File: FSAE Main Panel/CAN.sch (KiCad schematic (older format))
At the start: 8 parts, among them U401 MCP2515-I/ST, U402 MCP2551-I/SN, Y401 16MHz

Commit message: New footprints, finished associating footprints
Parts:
- Y401: footprint (none) -> CSTNE16M0V530000R0:CSTNE16M0V530000R0
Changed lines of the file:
@@
 F 0 "Y401" H 3400 3900 50  0000 C CNN
 F 1 "16MHz" H 3400 3600 50  0000 C CNN
-F 2 "" H 3400 3750 50  0001 C CNN
+F 2 "CSTNE16M0V530000R0:CSTNE16M0V530000R0" H 3400 3750 50  0001 C CNN
 F 3 "" H 3400 3750 50  0001 C CNN
 	1    3400 3750

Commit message: Edited footprints, started PCB layout
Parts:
- removed C401, C402: 22pF, Capacitors_SMD:C_1206, symbol Device:C
- removed Y401: 16MHz, CSTNE16M0V530000R0:CSTNE16M0V530000R0, symbol Device:Crystal
- added Y401: Resonator, CSTNE16M0V530000R0:CSTNE16M0V530000R0, symbol Device:Resonator
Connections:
- wire segments 38 -> 35
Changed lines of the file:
@@
 $EndComp
-$Comp
-L Device:Crystal Y401
-U 1 1 5BE251BE
-P 3400 3750
-F 0 "Y401" H 3400 3900 50  0000 C CNN
-F 1 "16MHz" H 3400 3600 50  0000 C CNN
-F 2 "CSTNE16M0V530000R0:CSTNE16M0V530000R0" H 3400 3750 50  0001 C CNN
-F 3 "" H 3400 3750 50  0001 C CNN
-	1    3400 3750
-	0    -1   -1   0
-$EndComp
-Wire Wire Line
-	3000 3600 3400 3600
-Wire Wire Line
-	4100 3700 3650 3700
-Wire Wire Line
-	3650 3700 3650 3900
-Wire Wire Line
-	3650 3900 3400 3900
-$Comp
-L Device:C C401
-U 1 1 5BE2525F
-P 2850 3600
-F 0 "C401" V 2750 3700 50  0000 L CNN
-F 1 "22pF" V 2750 3350 50  0000 L CNN
-F 2 "Capacitors_SMD:C_1206" H 2888 3450 50  0001 C CNN
-F 3 "" H 2850 3600 50  0001 C CNN
-F 4 "Ceramic 22pF 10V C0G/NG0 0805" V 2850 3600 50  0001 C CNN "Description"
-	1    2850 3600
-	0    1    1    0
-$EndComp
-$Comp
-L Device:C C402
-U 1 1 5BE2528F
-P 2850 3900
-F 0 "C402" V 2750 4000 50  0000 L CNN
-F 1 "22pF" V 2750 3650 50  0000 L CNN
-F 2 "Capacitors_SMD:C_1206" H 2888 3750 50  0001 C CNN
-F 3 "" H 2850 3900 50  0001 C CNN
-F 4 "Ceramic 22pF 10V C0G/NG0 0805" V 2850 3900 50  0001 C CNN "Description"
-	1    2850 3900
-	0    1    1    0
-$EndComp
-Connection ~ 3400 3600
-Connection ~ 3400 3900
 $Comp
 L power:GND #PWR0401
 U 1 1 5BE2541F
-P 2400 4600
-F 0 "#PWR0401" H 2400 4350 50  0001 C CNN
-F 1 "GND" H 2400 4450 50  0000 C CNN
-F 2 "" H 2400 4600 50  0001 C CNN
-F 3 "" H 2400 4600 50  0001 C CNN
-	1    2400 4600
+P 3400 4550
+F 0 "#PWR0401" H 3400 4300 50  0001 C CNN
+F 1 "GND" H 3400 4400 50  0000 C CNN
+F 2 "" H 3400 4550 50  0001 C CNN
+F 3 "" H 3400 4550 50  0001 C CNN
+	1    3400 4550
 	1    0    0    -1
 $EndComp
-Wire Wire Line
-	2700 3600 2400 3600
-Wire Wire Line
-	2400 3600 2400 3900
-Wire Wire Line
-	2700 3900 2400 3900
-Connection ~ 2400 3900
 $Comp
 L power:+3.3V #PWR0402
@@
 	4700 4200 4700 4350
 Wire Wire Line
-	4700 4350 2400 4350
-Connection ~ 2400 4350
+	4700 4350 3400 4350
 $Comp
 L FSAE-Main-Panel-rescue:MCP2551-I_SN U402
@@
 NoConn ~ 4100 3800
 Wire Wire Line
-	3400 3600 4100 3600
-Wire Wire Line
-	3400 3900 3000 3900
-Wire Wire Line
-	2400 3900 2400 4350
-Wire Wire Line
-	2400 4350 2400 4600
-Wire Wire Line
 	4700 2400 4700 2600
 Wire Wire Line
@@
 Wire Wire Line
 	6000 2400 7200 2400
+$Comp
+L Device:Resonator Y401
+U 1 1 5C382AA1
+P 3400 3700
+F 0 "Y401" H 3400 3948 50  0000 C CNN
+F 1 "Resonator" H 3400 3857 50  0000 C CNN
+F 2 "CSTNE16M0V530000R0:CSTNE16M0V530000R0" H 3375 3700 50  0001 C CNN
+F 3 "~" H 3375 3700 50  0001 C CNN
+	1    3400 3700
+	-1   0    0    -1
+$EndComp
+Wire Wire Line
+	3250 3700 3100 3700
+Wire Wire Line
+	3100 3700 3100 3300
+Wire Wire Line
+	3100 3300 3800 3300
+Wire Wire Line
+	3800 3300 3800 3600
+Wire Wire Line
+	3800 3600 4100 3600
+Wire Wire Line
+	3550 3700 4100 3700
+Connection ~ 3400 4350
+Wire Wire Line
+	3400 4350 3400 4550
+Wire Wire Line
+	3400 3900 3400 4350
 $EndSCHEMATC

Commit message: Updated PCB
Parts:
- U401: footprint Housings_SSOP:TSSOP-20_4.4x6.5mm_Pitch0.65mm -> Housings_SOIC:SOIC-18W_7.5x11.6mm_Pitch1.27mm; symbol FSAE-Main-Panel-rescue:MCP2515-I_ST -> Interface_CAN_LIN:MCP2515-xSO
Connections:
- net +3V3: now also U401.18 (VDD); no longer U401.20 (VDD)
- net CAN_CS: now also U401.16 (~CS); no longer U401.18 (~CS)
- net CAN_MISO: now also U401.15 (SO); no longer U401.17 (SO)
- net CAN_MOSI: now also U401.14 (SI); no longer U401.16 (SI)
- net CAN_SCLK: now also U401.13 (SCK); no longer U401.14 (SCK)
- net GND: now also U401.9 (VSS); no longer U401.10 (VSS)
- net at R401.2: now also U401.17 (~RESET); no longer U401.19 (~RESET)
- net at U401.7 (OSC2): now also Y401.3
- net at U401.8 (OSC1): now also Y401.1; no longer Y401.3
- no-connect marks 2 -> 8
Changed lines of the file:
@@
 $EndDescr
 $Comp
-L FSAE-Main-Panel-rescue:MCP2515-I_ST U401
+L Interface_CAN_LIN:MCP2515-xSO U401
 U 1 1 5BE2515F
 P 4700 3400
 F 0 "U401" H 4300 4175 50  0000 R CNN
 F 1 "MCP2515-I/ST" H 5450 4200 50  0000 R TNN
-F 2 "Housings_SSOP:TSSOP-20_4.4x6.5mm_Pitch0.65mm" H 4700 2500 50  0001 C CIN
+F 2 "Housings_SOIC:SOIC-18W_7.5x11.6mm_Pitch1.27mm" H 4700 2500 50  0001 C CIN
 F 3 "" H 4800 2600 50  0001 C CNN
 	1    4700 3400
@@
 Wire Wire Line
 	3400 3900 3400 4350
+NoConn ~ 5300 3400
+NoConn ~ 5300 3500
+NoConn ~ 5300 3600
+NoConn ~ 5300 3700
+NoConn ~ 5300 3800
+NoConn ~ 5300 3900
 $EndSCHEMATC

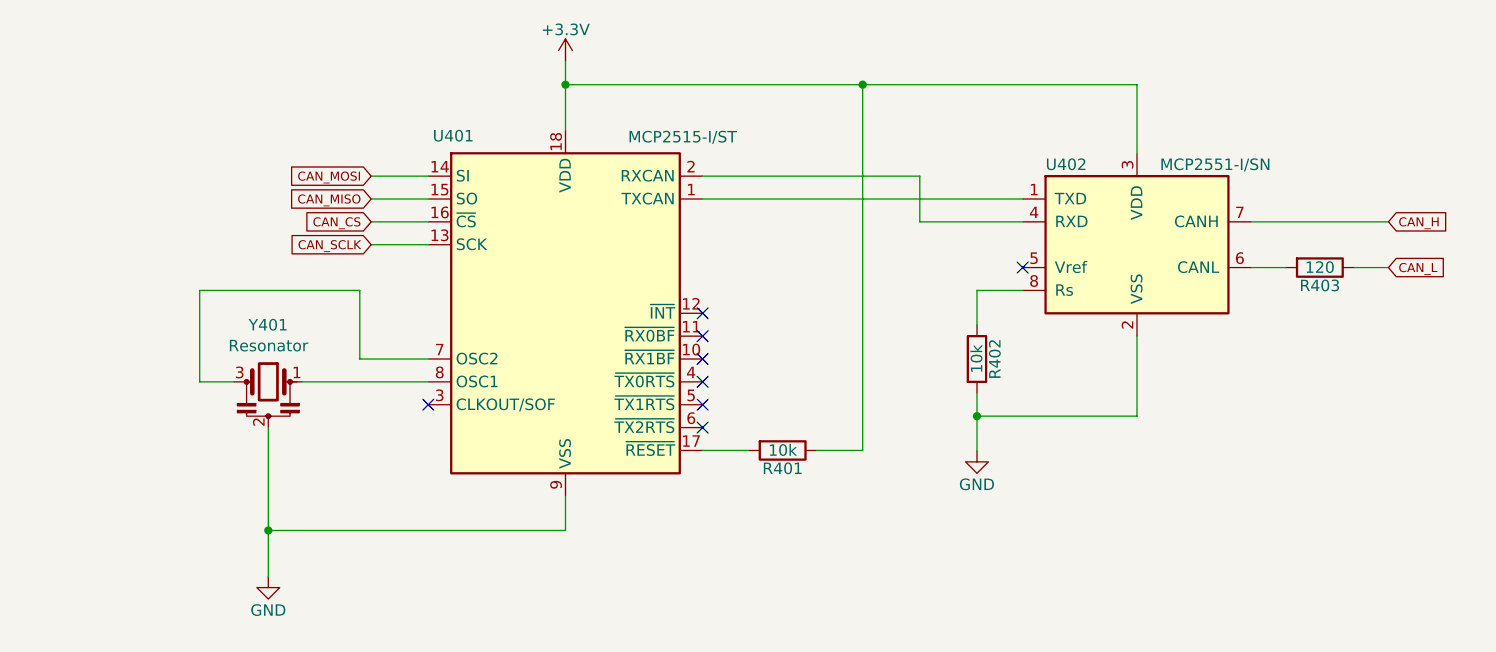
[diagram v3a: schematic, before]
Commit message: Major Revision
Deleted a ton of routes, Sorry Gary.
Changed all LEDs to 1206s for better brightness
Added a lot of local net names for easier routing
Flipped J203 for better routing
Expanded board outline to fit final dashboard cutout
Added half of the Mounting Holes
Realigned RPM strip
Added Linear Reg Load Resistors to meet minimum current specs
Changed Aux load Linear Regulators to a better one
Added Separate Linear Reg for the DWC
Tuned the CAN Bus differential Pair Lines for equal length
Added decoupling capacitors at a few locations
Rerouted Power traces to be shorter and cleaner
Set up keep out zones for CAN bus interference shielding.
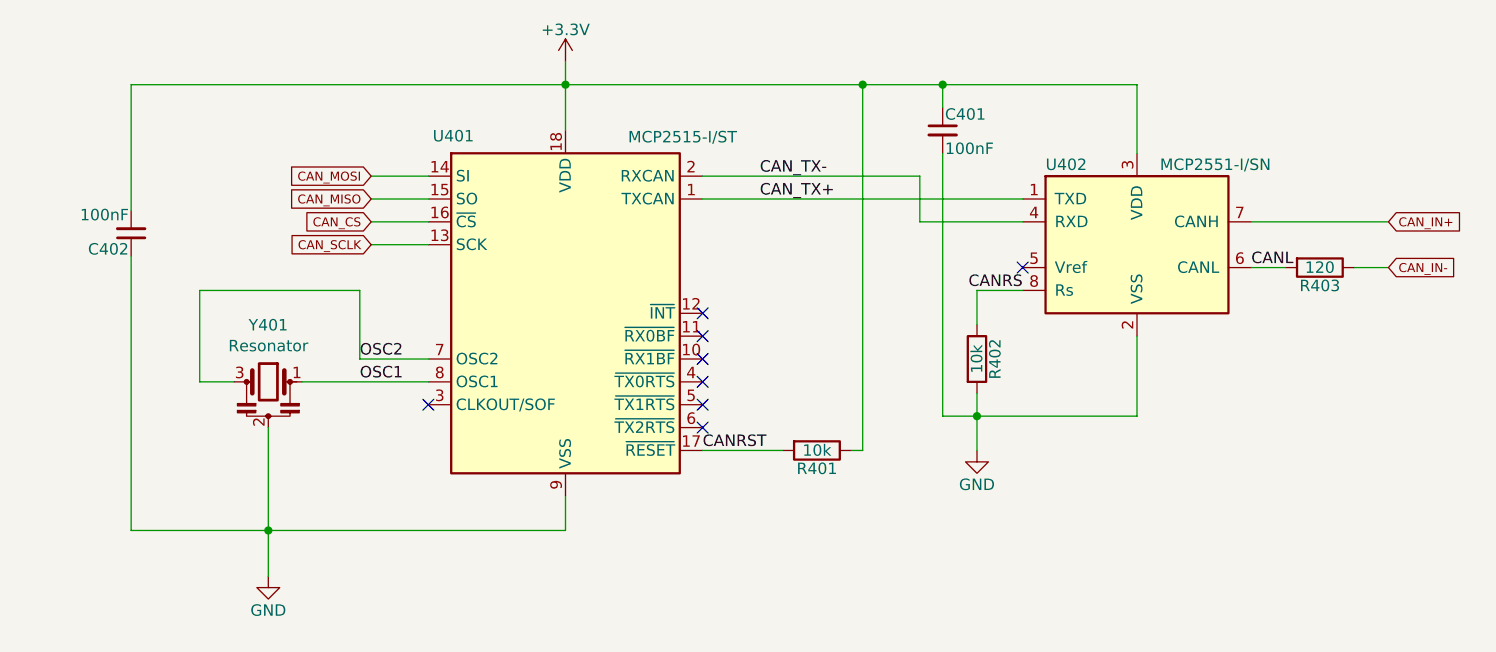
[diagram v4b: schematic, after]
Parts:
- added C401, C402: 100nF, Capacitors_SMD:C_1206, symbol Device:C_Small
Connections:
- net +3V3: now also C401.1, C402.2
- net GND: now also C401.2, C402.1
- net CAN_TX+: now reaches U401.1 (TXCAN), U402.1 (TXD)
- net CANRST: now reaches R401.2, U401.17 (~RESET)
- net CAN_TX-: now reaches U401.2 (RXCAN), U402.4 (RXD)
- net OSC2: now reaches U401.7 (OSC2), Y401.3
- net OSC1: now reaches U401.8 (OSC1), Y401.1
- net CANL: now reaches R403.2, U402.6 (CANL)
- net CANRS: now reaches R402.1, U402.8 (Rs)
- net CAN_H renamed CAN_IN+
- net CAN_L renamed CAN_IN-
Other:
- moved on the sheet: R401
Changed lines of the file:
@@
 L Device:R R401
 U 1 1 5BE255B1
-P 5650 4000
-F 0 "R401" V 5730 4000 50  0000 C CNN
-F 1 "10k" V 5650 4000 50  0000 C CNN
-F 2 "Resistors_SMD:R_1206" V 5580 4000 50  0001 C CNN
-F 3 "" H 5650 4000 50  0001 C CNN
-	1    5650 4000
+P 5800 4000
+F 0 "R401" V 5880 4000 50  0000 C CNN
+F 1 "10k" V 5800 4000 50  0000 C CNN
+F 2 "Resistors_SMD:R_1206" V 5730 4000 50  0001 C CNN
+F 3 "" H 5800 4000 50  0001 C CNN
+	1    5800 4000
 	0    1    1    0
 $EndComp
 Wire Wire Line
-	5500 4000 5300 4000
-Wire Wire Line
-	5800 4000 6000 4000
+	5650 4000 5300 4000
+Wire Wire Line
+	5950 4000 6000 4000
 Wire Wire Line
 	6000 4000 6000 2400
@@
 $EndComp
 Text GLabel 8300 3000 2    39   Input ~ 0
-CAN_H
+CAN_IN+
 Text GLabel 8300 3200 2    39   Input ~ 0
-CAN_L
+CAN_IN-
 Wire Wire Line
 	7700 3000 8300 3000
@@
 	6500 3850 6500 4000
 Wire Wire Line
-	6000 2400 7200 2400
+	6000 2400 6350 2400
 $Comp
 L Device:Resonator Y401
@@
 NoConn ~ 5300 3800
 NoConn ~ 5300 3900
+Text Label 5550 2800 0    50   ~ 0
+CAN_TX-
+Text Label 5550 2900 0    50   ~ 0
+CAN_TX+
+Text Label 3800 3600 0    50   ~ 0
+OSC2
+Text Label 3800 3700 0    50   ~ 0
+OSC1
+Text Label 6700 3300 2    50   ~ 0
+CANRS
+Text Label 7700 3200 0    50   ~ 0
+CANL
+Text Label 5300 4000 0    50   ~ 0
+CANRST
+$Comp
+L Device:C_Small C?
+U 1 1 5C806C3C
+P 6350 2600
+AR Path="/5C806C3C" Ref="C?"  Part="1"
+AR Path="/5BE25053/5C806C3C" Ref="C401"  Part="1"
+F 0 "C401" H 6360 2670 50  0000 L CNN
+F 1 "100nF" H 6360 2520 50  0000 L CNN
+F 2 "Capacitors_SMD:C_1206" H 6350 2600 50  0001 C CNN
+F 3 "" H 6350 2600 50  0001 C CNN
+F 4 "Ceramic 0.1uF 10V X7R 1206" H 6350 2600 50  0001 C CNN "Description"
+	1    6350 2600
+	1    0    0    -1
+$EndComp
+$Comp
+L Device:C_Small C?
+U 1 1 5C8072C7
+P 2800 3050
+AR Path="/5C8072C7" Ref="C?"  Part="1"
+AR Path="/5BE25053/5C8072C7" Ref="C402"  Part="1"
+F 0 "C402" H 2810 3120 50  0000 L CNN
+F 1 "100nF" H 2810 2970 50  0000 L CNN
+F 2 "Capacitors_SMD:C_1206" H 2800 3050 50  0001 C CNN
+F 3 "" H 2800 3050 50  0001 C CNN
+F 4 "Ceramic 0.1uF 10V X7R 1206" H 2800 3050 50  0001 C CNN "Description"
+	1    2800 3050
+	-1   0    0    1
+$EndComp
+Wire Wire Line
+	6350 2500 6350 2400
+Connection ~ 6350 2400
+Wire Wire Line
+	6350 2400 7200 2400
+Wire Wire Line
+	6350 2700 6350 3850
+Wire Wire Line
+	6350 3850 6500 3850
+Wire Wire Line
+	2800 2950 2800 2400
+Wire Wire Line
+	2800 2400 4700 2400
+Wire Wire Line
+	2800 4350 3400 4350
+Wire Wire Line
+	2800 3150 2800 4350
 $EndSCHEMATC

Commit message: Initial Fabrication
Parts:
- R402: value 10k -> 16.9k
- R403: footprint Resistors_SMD:R_1206 -> Resistors_SMD:R_0805
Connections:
- net +3V3: no longer C401.1, U402.3 (VDD)
- net CAN_IN+: now also R403.2
- net CAN_IN-: now also U402.6 (CANL)
- removed net CANL: R403.2, U402.6 (CANL)
- new net +5V: C401.1, U402.3 (VDD)
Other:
- moved on the sheet: R403
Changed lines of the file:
@@
 P 6500 3600
 F 0 "R402" V 6580 3600 50  0000 C CNN
-F 1 "10k" V 6500 3600 50  0000 C CNN
+F 1 "16.9k" V 6500 3600 50  0000 C CNN
 F 2 "Resistors_SMD:R_1206" V 6430 3600 50  0001 C CNN
 F 3 "" H 6500 3600 50  0001 C CNN
@@
 Wire Wire Line
 	7200 2400 7200 2700
-Connection ~ 6000 2400
 $Comp
 L Device:R R403
 U 1 1 5BE25A3B
-P 8000 3200
-F 0 "R403" V 8080 3200 50  0000 C CNN
-F 1 "120" V 8000 3200 50  0000 C CNN
-F 2 "Resistors_SMD:R_1206" V 7930 3200 50  0001 C CNN
-F 3 "" H 8000 3200 50  0001 C CNN
-	1    8000 3200
-	0    1    1    0
+P 8050 3150
+F 0 "R403" V 8150 3150 50  0000 C CNN
+F 1 "120" V 8050 3150 50  0000 C CNN
+F 2 "Resistors_SMD:R_0805" V 7980 3150 50  0001 C CNN
+F 3 "" H 8050 3150 50  0001 C CNN
+	1    8050 3150
+	-1   0    0    1
 $EndComp
 Text GLabel 8300 3000 2    39   Input ~ 0
 CAN_IN+
-Text GLabel 8300 3200 2    39   Input ~ 0
+Text GLabel 8300 3300 2    39   Input ~ 0
 CAN_IN-
 Wire Wire Line
-	7700 3000 8300 3000
-Wire Wire Line
-	7700 3200 7850 3200
-Wire Wire Line
-	8150 3200 8300 3200
+	7700 3000 8050 3000
 Text GLabel 3850 3100 0    39   Input ~ 0
 CAN_SCLK
@@
 Wire Wire Line
 	6500 3850 6500 4000
-Wire Wire Line
-	6000 2400 6350 2400
 $Comp
 L Device:Resonator Y401
@@
 Wire Wire Line
 	6350 2500 6350 2400
-Connection ~ 6350 2400
 Wire Wire Line
 	6350 2400 7200 2400
@@
 Wire Wire Line
 	2800 3150 2800 4350
+Connection ~ 8050 3000
+Wire Wire Line
+	8050 3000 8300 3000
+Wire Wire Line
+	8050 3300 8300 3300
+Wire Wire Line
+	8050 3300 7700 3300
+Wire Wire Line
+	7700 3300 7700 3200
+Connection ~ 8050 3300
+$Comp
+L power:+5V #PWR?
+U 1 1 5C932133
+P 6350 2400
+F 0 "#PWR?" H 6350 2250 50  0001 C CNN
+F 1 "+5V" H 6365 2573 50  0000 C CNN
+F 2 "" H 6350 2400 50  0001 C CNN
+F 3 "" H 6350 2400 50  0001 C CNN
+	1    6350 2400
+	1    0    0    -1
+$EndComp
+Connection ~ 6350 2400
 $EndSCHEMATC

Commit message: Updated attributes and BOM
Standardized the component attributes and BOM.

Some errors were identified and will be corrected in the next board revision
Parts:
- C401, C402: Description Ceramic 0.1uF 10V X7R 1206 -> CAP CER 0.1UF 25V X7R 1206; Manufacturer (none) -> KEMET; Part Number (none) -> C1206F104K3RACTU
- R401: Description (none) -> RES 10K OHM 5% 1/4W 1206; Manufacturer (none) -> Stackpole; Part Number (none) -> RMCF1206JT10K0
- R402: Description (none) -> RES 16.9K OHM 1% 1/4W 1206; Manufacturer (none) -> Stackpole; Part Number (none) -> RMCF1206FT16K9
- R403: Description (none) -> RES 120 OHM 1% 1/8W 0805; Manufacturer (none) -> Stackpole; Part Number (none) -> RMCF0805FT120R
- U401: Description (none) -> IC CAN CONTROLLER W/SPI 20TSSOP; Manufacturer (none) -> Microchip; Part Number (none) -> MCP2515-I/ST
- U402: Description (none) -> IC TRANSCEIVER CAN HI-SPD 8-SOIC; Manufacturer (none) -> Microchip; Part Number (none) -> MCP2551T-I/SN
- Y401: Description (none) -> CER RES 16.0000MHZ 15PF SMD; Manufacturer (none) -> Murata; Part Number (none) -> CSTNE16M0V530000R0
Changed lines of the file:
@@
 F 1 "MCP2515-I/ST" H 5450 4200 50  0000 R TNN
 F 2 "Housings_SOIC:SOIC-18W_7.5x11.6mm_Pitch1.27mm" H 4700 2500 50  0001 C CIN
-F 3 "" H 4800 2600 50  0001 C CNN
+F 3 "http://ww1.microchip.com/downloads/en/DeviceDoc/MCP2515-Stand-Alone-CAN-Controller-with-SPI-20001801J.pdf" H 4800 2600 50  0001 C CNN
+F 4 "IC CAN CONTROLLER W/SPI 20TSSOP" H 0   0   50  0001 C CNN "Description"
+F 5 "Microchip" H 0   0   50  0001 C CNN "Manufacturer"
+F 6 "MCP2515-I/ST" H 0   0   50  0001 C CNN "Part Number"
 	1    4700 3400
 	1    0    0    -1
@@
 F 1 "MCP2551-I/SN" H 7300 3450 50  0000 L CNN
 F 2 "Housings_SOIC:SOIC-8_3.9x4.9mm_Pitch1.27mm" H 7200 2600 50  0001 C CIN
-F 3 "" H 7200 3100 50  0001 C CNN
+F 3 "http://ww1.microchip.com/downloads/en/DeviceDoc/20001667G.pdf" H 7200 3100 50  0001 C CNN
+F 4 "IC TRANSCEIVER CAN HI-SPD 8-SOIC" H 0   0   50  0001 C CNN "Description"
+F 5 "Microchip" H 0   0   50  0001 C CNN "Manufacturer"
+F 6 "MCP2551T-I/SN" H 0   0   50  0001 C CNN "Part Number"
 	1    7200 3100
 	1    0    0    -1
@@
 F 1 "10k" V 5800 4000 50  0000 C CNN
 F 2 "Resistors_SMD:R_1206" V 5730 4000 50  0001 C CNN
-F 3 "" H 5800 4000 50  0001 C CNN
+F 3 "https://www.seielect.com/catalog/sei-rmcf_rmcp.pdf" H 5800 4000 50  0001 C CNN
+F 4 "RES 10K OHM 5% 1/4W 1206" H 0   0   50  0001 C CNN "Description"
+F 5 "Stackpole" H 0   0   50  0001 C CNN "Manufacturer"
+F 6 "RMCF1206JT10K0" H 0   0   50  0001 C CNN "Part Number"
 	1    5800 4000
 	0    1    1    0
@@
 F 1 "16.9k" V 6500 3600 50  0000 C CNN
 F 2 "Resistors_SMD:R_1206" V 6430 3600 50  0001 C CNN
-F 3 "" H 6500 3600 50  0001 C CNN
+F 3 "https://www.seielect.com/catalog/sei-rmcf_rmcp.pdf" H 6500 3600 50  0001 C CNN
+F 4 "RES 16.9K OHM 1% 1/4W 1206" H 0   0   50  0001 C CNN "Description"
+F 5 "Stackpole" H 0   0   50  0001 C CNN "Manufacturer"
+F 6 "RMCF1206FT16K9" H 0   0   50  0001 C CNN "Part Number"
 	1    6500 3600
 	1    0    0    -1
@@
 F 1 "120" V 8050 3150 50  0000 C CNN
 F 2 "Resistors_SMD:R_0805" V 7980 3150 50  0001 C CNN
-F 3 "" H 8050 3150 50  0001 C CNN
+F 3 "https://www.seielect.com/catalog/sei-rmcf_rmcp.pdf" H 8050 3150 50  0001 C CNN
+F 4 "RES 120 OHM 1% 1/8W 0805" H 0   0   50  0001 C CNN "Description"
+F 5 "Stackpole" H 0   0   50  0001 C CNN "Manufacturer"
+F 6 "RMCF0805FT120R" H 0   0   50  0001 C CNN "Part Number"
 	1    8050 3150
 	-1   0    0    1
@@
 F 1 "Resonator" H 3400 3857 50  0000 C CNN
 F 2 "CSTNE16M0V530000R0:CSTNE16M0V530000R0" H 3375 3700 50  0001 C CNN
-F 3 "~" H 3375 3700 50  0001 C CNN
+F 3 "https://www.murata.com/en/products/productdata/8801162231838/SPEC-CSTNE16M0V530000R0.pdf" H 3375 3700 50  0001 C CNN
+F 4 "CER RES 16.0000MHZ 15PF SMD" H 0   0   50  0001 C CNN "Description"
+F 5 "Murata" H 0   0   50  0001 C CNN "Manufacturer"
+F 6 "	CSTNE16M0V530000R0" H 0   0   50  0001 C CNN "Part Number"
 	1    3400 3700
 	-1   0    0    -1
@@
 F 1 "100nF" H 6360 2520 50  0000 L CNN
 F 2 "Capacitors_SMD:C_1206" H 6350 2600 50  0001 C CNN
-F 3 "" H 6350 2600 50  0001 C CNN
-F 4 "Ceramic 0.1uF 10V X7R 1206" H 6350 2600 50  0001 C CNN "Description"
+F 3 "https://content.kemet.com/datasheets/KEM_C1012_X7R_OPENMODE_SMD.pdf" H 6350 2600 50  0001 C CNN
+F 4 "CAP CER 0.1UF 25V X7R 1206" H 6350 2600 50  0001 C CNN "Description"
+F 5 "KEMET" H 0   0   50  0001 C CNN "Manufacturer"
+F 6 "C1206F104K3RACTU" H 0   0   50  0001 C CNN "Part Number"
 	1    6350 2600
 	1    0    0    -1
@@
 F 1 "100nF" H 2810 2970 50  0000 L CNN
 F 2 "Capacitors_SMD:C_1206" H 2800 3050 50  0001 C CNN
-F 3 "" H 2800 3050 50  0001 C CNN
-F 4 "Ceramic 0.1uF 10V X7R 1206" H 2800 3050 50  0001 C CNN "Description"
+F 3 "https://content.kemet.com/datasheets/KEM_C1012_X7R_OPENMODE_SMD.pdf" H 2800 3050 50  0001 C CNN
+F 4 "CAP CER 0.1UF 25V X7R 1206" H 2800 3050 50  0001 C CNN "Description"
+F 5 "KEMET" H 0   0   50  0001 C CNN "Manufacturer"
+F 6 "C1206F104K3RACTU" H 0   0   50  0001 C CNN "Part Number"
 	1    2800 3050
 	-1   0    0    1
@@
 Connection ~ 8050 3300
 $Comp
-L power:+5V #PWR?
+L power:+5V #PWR0116
 U 1 1 5C932133
 P 6350 2400
-F 0 "#PWR?" H 6350 2250 50  0001 C CNN
+F 0 "#PWR0116" H 6350 2250 50  0001 C CNN
 F 1 "+5V" H 6365 2573 50  0000 C CNN
 F 2 "" H 6350 2400 50  0001 C CNN

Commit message: Dashboard test code
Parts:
- U402: symbol FSAE-Main-Panel-rescue:MCP2551-I_SN -> Interface_CAN_LIN:MCP2551-I-SN
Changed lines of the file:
@@
 	4700 4350 3400 4350
 $Comp
-L FSAE-Main-Panel-rescue:MCP2551-I_SN U402
+L Interface_CAN_LIN:MCP2551-I-SN U402
 U 1 1 5BE25501
 P 7200 3100
